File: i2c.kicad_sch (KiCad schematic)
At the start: 22 parts, among them U16 PCA9517A_TSSOP, U23 TS5A3359_VSSOP, U24 TS5A3359_VSSOP

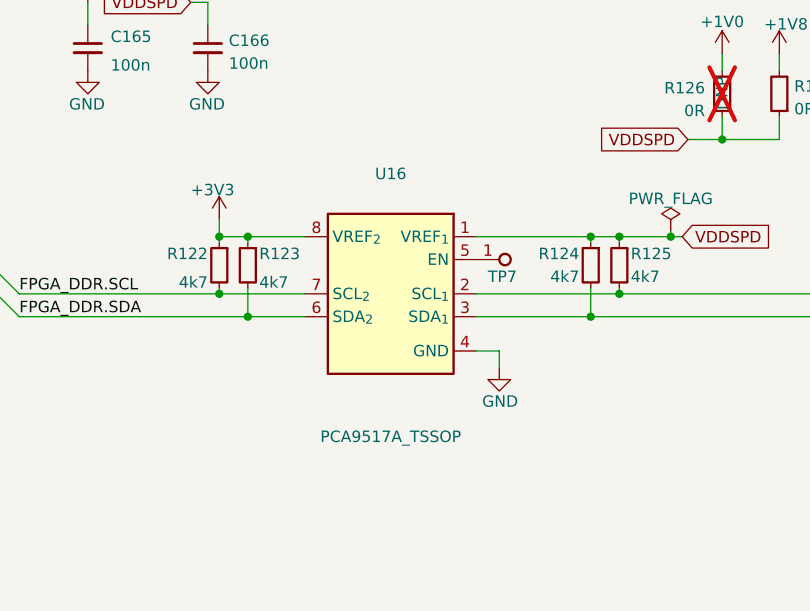
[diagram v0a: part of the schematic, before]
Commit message: [#58418] Update obsolete MPNs. Replace fuses. Remap PWR_EN and PWR_GOOD. Add UART logic level conventers. Bump revision to 1.2.0
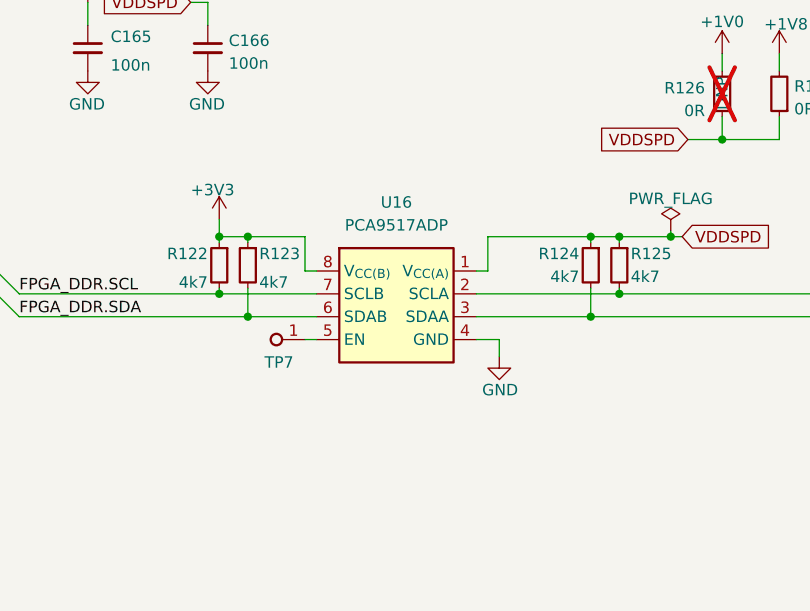
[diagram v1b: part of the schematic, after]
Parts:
- removed U16: PCA9517A_TSSOP, antmicro-footprints:TSSOP-8_3x3mm_P0.65mm, symbol antmicroLogicTranslatorsLevelShifters:PCA9517A_TSSOP
- added U16: PCA9517ADP, antmicro-footprints:TSSOP-8_3x3mm_P0.65mm, symbol antmicroLogicTranslatorsLevelShifters:PCA9517ADP
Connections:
- net +3V3: now also U16.8 (V_{CC(B)})
- net DDR.SCL: now also U16.2 (SCLA)
- net DDR.SDA: now also U16.3 (SDAA)
- net FPGA_DDR.SCL: now also U16.7 (SCLB)
- net FPGA_DDR.SDA: now also U16.6 (SDAB)
- net GND: now also U16.4 (GND)
- net VDDSPD: now also U16.1 (V_{CC(A)})
- net at TP7.1: now also U16.5 (EN)
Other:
- moved on the sheet: TP7
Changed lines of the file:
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@@
   (title_block
     (title "SO-DIMM DDR5 Tester")
-    (date "2024-01-18")
-    (rev "1.1.1:7ba41")
+    (date "2024-04-23")
+    (rev "1.2.0")
     (comment 1 "www.antmicro.com")
     (comment 2 "Antmicro Ltd")
@@
     (stroke (width 0) (type default))
   )
-  (wire (pts (xy 200.66 85.09) (xy 191.135 85.09))
-    (stroke (width 0) (type default))
-  )
-  (wire (pts (xy 219.71 78.74) (xy 232.41 78.74))
+  (wire (pts (xy 201.93 85.09) (xy 191.135 85.09))
+    (stroke (width 0) (type default))
+  )
+  (wire (pts (xy 200.66 82.55) (xy 201.93 82.55))
     (stroke (width 0) (type default))
   )
@@
     (stroke (width 0) (type default))
   )
-  (wire (pts (xy 222.25 91.44) (xy 219.71 91.44))
+  (wire (pts (xy 222.25 90.17) (xy 219.71 90.17))
     (stroke (width 0) (type default))
   )
@@
     (stroke (width 0) (type default))
   )
+  (wire (pts (xy 220.98 78.74) (xy 232.41 78.74))
+    (stroke (width 0) (type default))
+  )
   (bus (pts (xy 247.015 193.675) (xy 247.65 194.31))
     (stroke (width 0) (type default))
@@
     (stroke (width 0) (type default))
   )
-  (wire (pts (xy 222.25 91.44) (xy 222.25 93.345))
+  (wire (pts (xy 222.25 90.17) (xy 222.25 92.075))
     (stroke (width 0) (type default))
   )
@@
     (stroke (width 0) (type default))
   )
-  (wire (pts (xy 194.31 87.63) (xy 200.66 87.63))
+  (wire (pts (xy 194.31 87.63) (xy 201.93 87.63))
     (stroke (width 0) (type default))
   )
@@
     (stroke (width 0) (type default))
   )
+  (wire (pts (xy 219.71 82.55) (xy 220.98 82.55))
+    (stroke (width 0) (type default))
+  )
   (polyline (pts (xy 162.56 231.775) (xy 162.56 247.015))
     (stroke (width 0) (type default))
@@
     (stroke (width 0) (type default))
   )
+  (wire (pts (xy 200.66 90.17) (xy 201.93 90.17))
+    (stroke (width 0) (type default))
+  )
   (bus (pts (xy 265.43 191.77) (xy 265.43 193.675))
     (stroke (width 0) (type default))
@@
   )
   (wire (pts (xy 64.77 191.77) (xy 143.51 191.77))
+    (stroke (width 0) (type default))
+  )
+  (wire (pts (xy 200.66 78.74) (xy 200.66 82.55))
     (stroke (width 0) (type default))
   )
@@
   )
   (wire (pts (xy 247.015 58.42) (xy 247.015 60.325))
+    (stroke (width 0) (type default))
+  )
+  (wire (pts (xy 220.98 82.55) (xy 220.98 78.74))
     (stroke (width 0) (type default))
   )
@@
     )
   )
-  (symbol (lib_id "antmicroTestPoints:TP_1mm_SMD") (at 219.71 81.28 0) (mirror x) (unit 1)
+  (symbol (lib_id "antmicroTestPoints:TP_1mm_SMD") (at 200.66 90.17 0) (mirror y) (unit 1)
     (in_bom yes) (on_board yes) (dnp no)
-    (property "Reference" "TP7" (at 220.98 83.185 0)
+    (property "Reference" "TP7" (at 199.39 92.71 0)
       (effects (font (size 1.27 1.27)) (justify left))
     )
-    (property "Value" "TP_1mm_SMD" (at 234.95 73.66 0)
-      (effects (font (size 1.27 1.27) (thickness 0.15)) (justify left bottom) hide)
-    )
-    (property "Footprint" "antmicro-footprints:TP_SMD_1mm" (at 234.95 71.12 0)
-      (effects (font (size 1.27 1.27) (thickness 0.15)) (justify left bottom) hide)
-    )
-    (property "Datasheet" "" (at 234.95 68.58 0)
-      (effects (font (size 1.27 1.27) (thickness 0.15)) (justify left bottom) hide)
-    )
-    (property "MPN" "" (at 219.71 81.28 0)
-      (effects (font (size 1.27 1.27)) hide)
-    )
-    (property "Manufacturer" "" (at 219.71 81.28 0)
-      (effects (font (size 1.27 1.27)) hide)
-    )
-    (property "Author" "Antmicro" (at 234.95 66.04 0)
-      (effects (font (size 1.27 1.27) (thickness 0.15)) (justify left bottom) hide)
-    )
-    (property "License" "Apache-2.0" (at 234.95 63.5 0)
+    (property "Value" "TP_1mm_SMD" (at 185.42 97.79 0)
+      (effects (font (size 1.27 1.27) (thickness 0.15)) (justify left bottom) hide)
+    )
+    (property "Footprint" "antmicro-footprints:TP_SMD_1mm" (at 185.42 100.33 0)
+      (effects (font (size 1.27 1.27) (thickness 0.15)) (justify left bottom) hide)
+    )
+    (property "Datasheet" "" (at 185.42 102.87 0)
+      (effects (font (size 1.27 1.27) (thickness 0.15)) (justify left bottom) hide)
+    )
+    (property "MPN" "" (at 200.66 90.17 0)
+      (effects (font (size 1.27 1.27)) hide)
+    )
+    (property "Manufacturer" "" (at 200.66 90.17 0)
+      (effects (font (size 1.27 1.27)) hide)
+    )
+    (property "Author" "Antmicro" (at 185.42 105.41 0)
+      (effects (font (size 1.27 1.27) (thickness 0.15)) (justify left bottom) hide)
+    )
+    (property "License" "Apache-2.0" (at 185.42 107.95 0)
       (effects (font (size 1.27 1.27) (thickness 0.15)) (justify left bottom) hide)
     )
@@
     )
   )
+  (symbol (lib_id "antmicroLogicTranslatorsLevelShifters:PCA9517ADP") (at 219.71 82.55 0) (mirror y) (unit 1)
+    (in_bom yes) (on_board yes) (dnp no)
+    (property "Reference" "U16" (at 210.82 74.93 0)
+      (effects (font (size 1.27 1.27) (thickness 0.15)))
+    )
+    (property "Value" "PCA9517ADP" (at 210.82 77.47 0)
+      (effects (font (size 1.27 1.27) (thickness 0.15)))
+    )
+    (property "Footprint" "antmicro-footprints:TSSOP-8_3x3mm_P0.65mm" (at 186.69 90.17 0)
+      (effects (font (size 1.27 1.27) (thickness 0.15)) (justify left bottom) hide)
+    )
+    (property "Datasheet" "https://www.nxp.com/docs/en/data-sheet/PCA9517A.pdf" (at 186.69 92.71 0)
+      (effects (font (size 1.27 1.27) (thickness 0.15)) (justify left bottom) hide)
+    )
+    (property "MPN" "PCA9517ADP,118" (at 186.69 95.25 0)
+      (effects (font (size 1.27 1.27) (thickness 0.15)) (justify left bottom) hide)
+    )
+    (property "Manufacturer" "NXP" (at 186.69 97.79 0)
+      (effects (font (size 1.27 1.27) (thickness 0.15)) (justify left bottom) hide)
+    )
+    (property "Author" "Antmicro" (at 186.69 100.33 0)
+      (effects (font (size 1.27 1.27) (thickness 0.15)) (justify left bottom) hide)
+    )
+    (property "License" "Apache-2.0" (at 186.69 102.87 0)
+      (effects (font (size 1.27 1.27) (thickness 0.15)) (justify left bottom) hide)
+    )
+    (pin "1")
+    (pin "3")
+    (pin "7")
+    (pin "5")
+    (pin "2")
+    (pin "4")
+    (pin "8")
+    (pin "6")
+    (instances
+      (project "sodimm-ddr5-tester"
+        (path "/1faa6543-e26a-4449-8bac-ee14b9f19e5f/3f0d6799-172b-44a7-b59e-98d6f5f3049b"
+          (reference "U16") (unit 1)
+        )
+      )
+    )
+  )
   (symbol (lib_id "antmicropower:+1V8") (at 253.365 58.42 0) (mirror y) (unit 1)
     (in_bom yes) (on_board yes) (dnp no) (fields_autoplaced)
@@
     )
   )
-  (symbol (lib_id "antmicropower:GND") (at 222.25 93.345 0) (unit 1)
+  (symbol (lib_id "antmicropower:GND") (at 222.25 92.075 0) (unit 1)
     (in_bom yes) (on_board yes) (dnp no) (fields_autoplaced)
-    (property "Reference" "#PWR0271" (at 222.25 99.695 0)
-      (effects (font (size 1.27 1.27)) hide)
-    )
-    (property "Value" "GND" (at 220.345 97.79 0)
+    (property "Reference" "#PWR0271" (at 222.25 98.425 0)
+      (effects (font (size 1.27 1.27)) hide)
+    )
+    (property "Value" "GND" (at 220.345 96.52 0)
       (effects (font (size 1.27 1.27) (thickness 0.15)) (justify left bottom))
     )
-    (property "Footprint" "" (at 231.14 100.965 0)
-      (effects (font (size 1.27 1.27) (thickness 0.15)) (justify left bottom) hide)
-    )
-    (property "Datasheet" "" (at 231.14 106.045 0)
-      (effects (font (size 1.27 1.27) (thickness 0.15)) (justify left bottom) hide)
-    )
-    (property "Author" "Antmicro" (at 231.14 98.425 0)
-      (effects (font (size 1.27 1.27) (thickness 0.15)) (justify left bottom) hide)
-    )
-    (property "License" "Apache-2.0" (at 231.14 100.965 0)
+    (property "Footprint" "" (at 231.14 99.695 0)
+      (effects (font (size 1.27 1.27) (thickness 0.15)) (justify left bottom) hide)
+    )
+    (property "Datasheet" "" (at 231.14 104.775 0)
+      (effects (font (size 1.27 1.27) (thickness 0.15)) (justify left bottom) hide)
+    )
+    (property "Author" "Antmicro" (at 231.14 97.155 0)
+      (effects (font (size 1.27 1.27) (thickness 0.15)) (justify left bottom) hide)
+    )
+    (property "License" "Apache-2.0" (at 231.14 99.695 0)
       (effects (font (size 1.27 1.27) (thickness 0.15)) (justify left bottom) hide)
     )
@@
         )
       )
-    )
-  )
-  (symbol (lib_id "antmicroLogicTranslatorsLevelShifters:PCA9517A_TSSOP") (at 219.71 78.74 0) (mirror y) (unit 1)
-    (in_bom yes) (on_board yes) (dnp no)
-    (property "Reference" "U16" (at 210.185 71.755 0)
-      (effects (font (size 1.27 1.27)))
-    )
-    (property "Value" "PCA9517A_TSSOP" (at 210.185 100.965 0)
-      (effects (font (size 1.27 1.27) (thickness 0.15)))
-    )
-    (property "Footprint" "antmicro-footprints:TSSOP-8_3x3mm_P0.65mm" (at 186.69 86.36 0)
-      (effects (font (size 1.27 1.27) (thickness 0.15)) (justify left bottom) hide)
-    )
-    (property "Datasheet" "https://www.mouser.com/datasheet/2/308/1/ONSM_S_A0009688870_1-2560458.pdf" (at 186.69 88.9 0)
-      (effects (font (size 1.27 1.27) (thickness 0.15)) (justify left bottom) hide)
-    )
-    (property "MPN" "PCA9517ADMR2G" (at 210.185 74.295 0)
-      (effects (font (size 1.27 1.27) (thickness 0.15)) hide)
-    )
-    (property "Manufacturer" "ON Semiconductor" (at 186.69 93.98 0)
-      (effects (font (size 1.27 1.27) (thickness 0.15)) (justify left bottom) hide)
-    )
-    (property "Author" "Antmicro" (at 186.69 96.52 0)
-      (effects (font (size 1.27 1.27) (thickness 0.15)) (justify left bottom) hide)
-    )
-    (property "License" "Apache-2.0" (at 186.69 99.06 0)
-      (effects (font (size 1.27 1.27) (thickness 0.15)) (justify left bottom) hide)
-    )
-    (pin "1")
-    (pin "2")
-    (pin "3")
-    (pin "4")
-    (pin "5")
-    (pin "6")
-    (pin "7")
-    (pin "8")
-    (instances
-      (project "sodimm-ddr5-tester"
-        (path "/1faa6543-e26a-4449-8bac-ee14b9f19e5f/3f0d6799-172b-44a7-b59e-98d6f5f3049b"
-          (reference "U16") (unit 1)
-        )
-      )

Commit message: [#86301] Project refresh 81589
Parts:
- R126, R174, R175, R176, R177, R178, R179: DNP DNP -> (none)

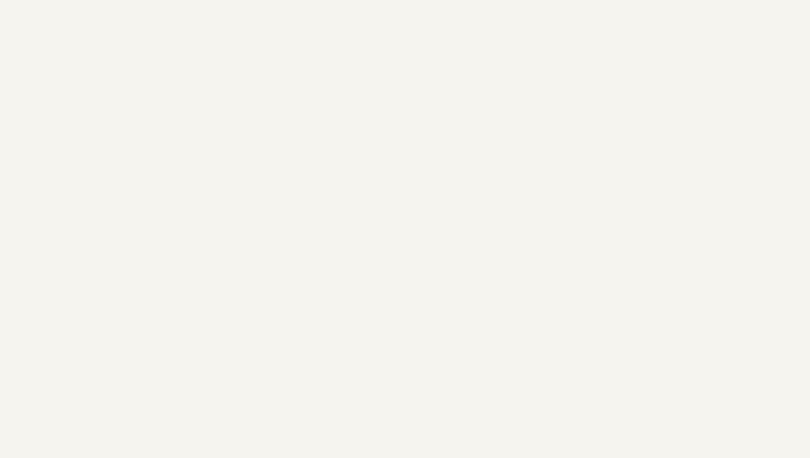
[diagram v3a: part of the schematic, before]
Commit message: [#87036] Add IC testpoints
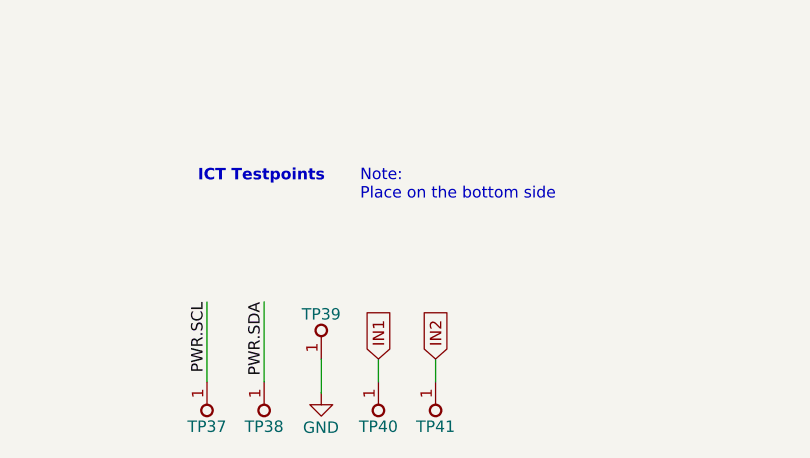
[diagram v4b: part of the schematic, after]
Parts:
- added TP37, TP38, TP39, TP40, TP41: TP_1mm_SMD, antmicro-footprints:TP_SMD_1mm, symbol antmicroTestPoints:TP_1mm_SMD
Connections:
- net GND: now also TP39.1
- net IN1: now also TP40.1
- net IN2: now also TP41.1
- net PWR.SCL: now also TP37.1
- net PWR.SDA: now also TP38.1
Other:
- note added: "ICT Testpoints"
- note added: "Note: Place on the bottom side"
- company: (none) -> Antmicro Ltd.

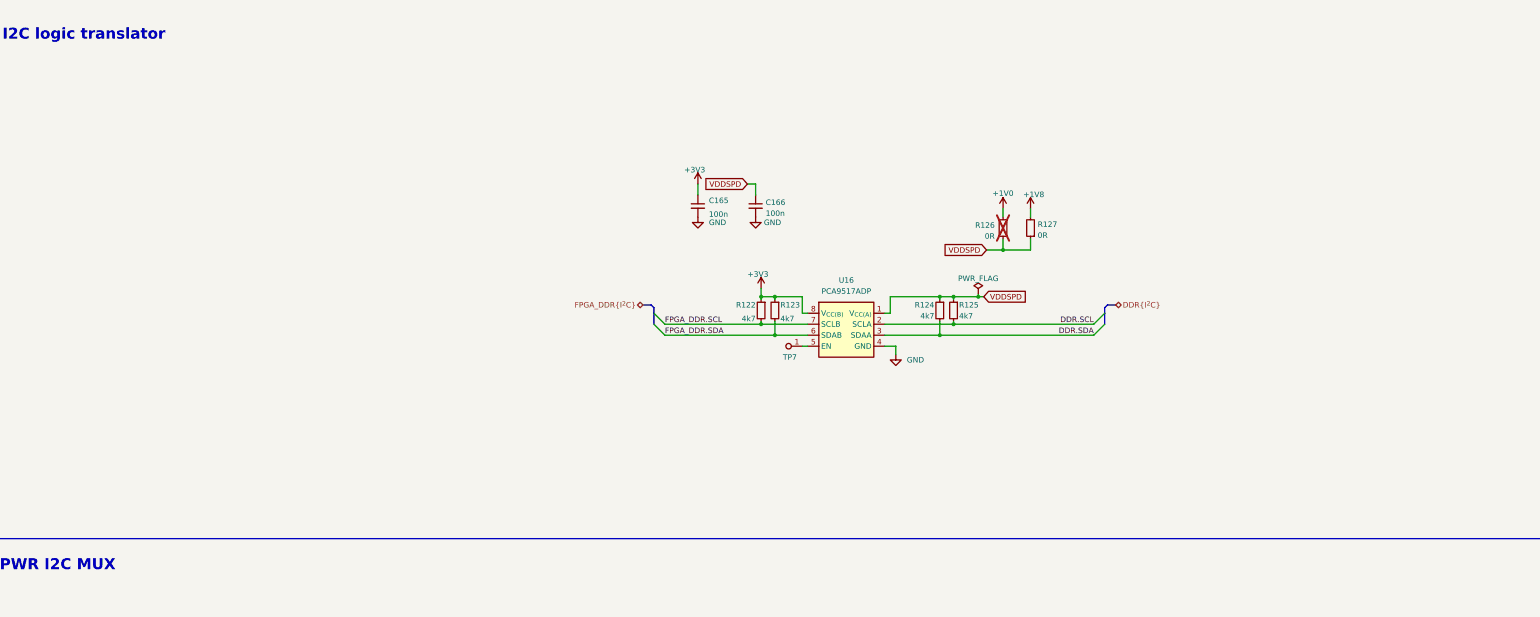
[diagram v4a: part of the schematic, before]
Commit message: [#87036] Add EEPROM with unique ID
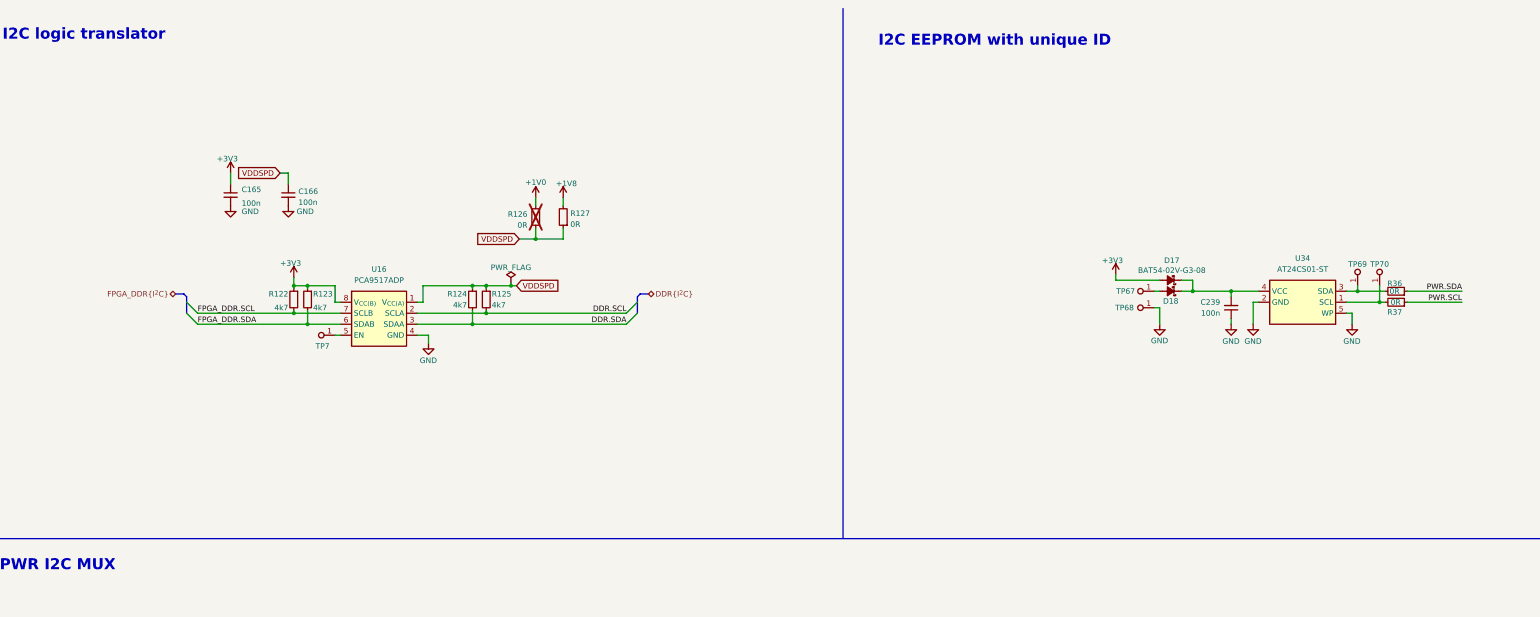
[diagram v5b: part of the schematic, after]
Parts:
- added C239: C_100n_0402, antmicro-footprints:C_0402_1005Metric, symbol antmicroCapacitors0402:C_100n_0402
- added D17, D18: BAT54-02V-G3-08, antmicro-footprints:SOD-523, symbol antmicroDiodesRectifiersSingle:BAT54-02V-G3-08
- added R36, R37: R_0R_0402, antmicro-footprints:R_0402_1005Metric, symbol antmicroResistors0402:R_0R_0402
- added TP67, TP68, TP69, TP70: TP_1mm_SMD, antmicro-footprints:TP_SMD_1mm, symbol antmicroTestPoints:TP_1mm_SMD
- added U34: AT24CS01_SOT23, antmicro-footprints:SOT-23-5, symbol antmicroMemory:AT24CS01_SOT23
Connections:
- net +3V3: now also D17.2 (A)
- net GND: now also C239.1, TP68.1, U34.2 (GND), U34.5 (WP)
- net PWR.SCL: now also R37.1
- net PWR.SDA: now also R36.1
- new net: R36.2, TP69.1, U34.3 (SDA)
- new net: C239.2, D17.1 (C), D18.1 (C), U34.4 (VCC)
- new net: D18.2 (A), TP67.1
- new net: R37.2, TP70.1, U34.1 (SCL)
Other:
- note added: "I2C EEPROM with unique ID"
- moved on the sheet: C165, C166, R122, R123, R124, R125, R126, R127, TP7, U16
